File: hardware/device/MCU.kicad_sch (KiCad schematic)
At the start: 20 parts, among them J4 EXPANSION, SW24 NRST, U18 STM32H743ZIT6

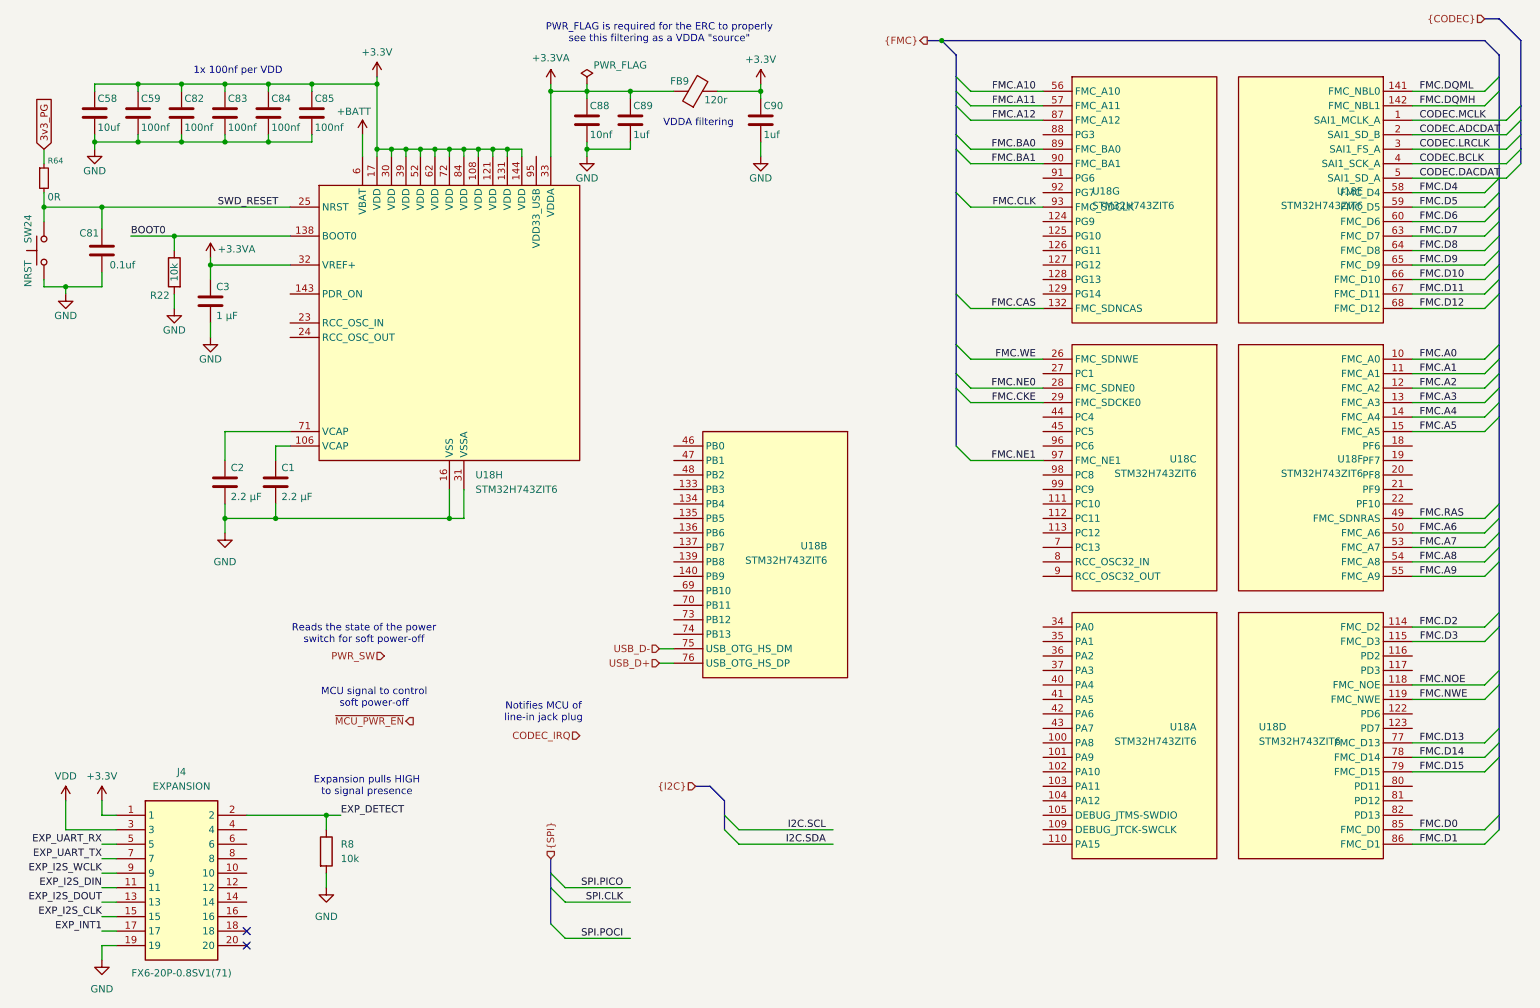
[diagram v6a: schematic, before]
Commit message: feat: change codec to NAU88C22YG
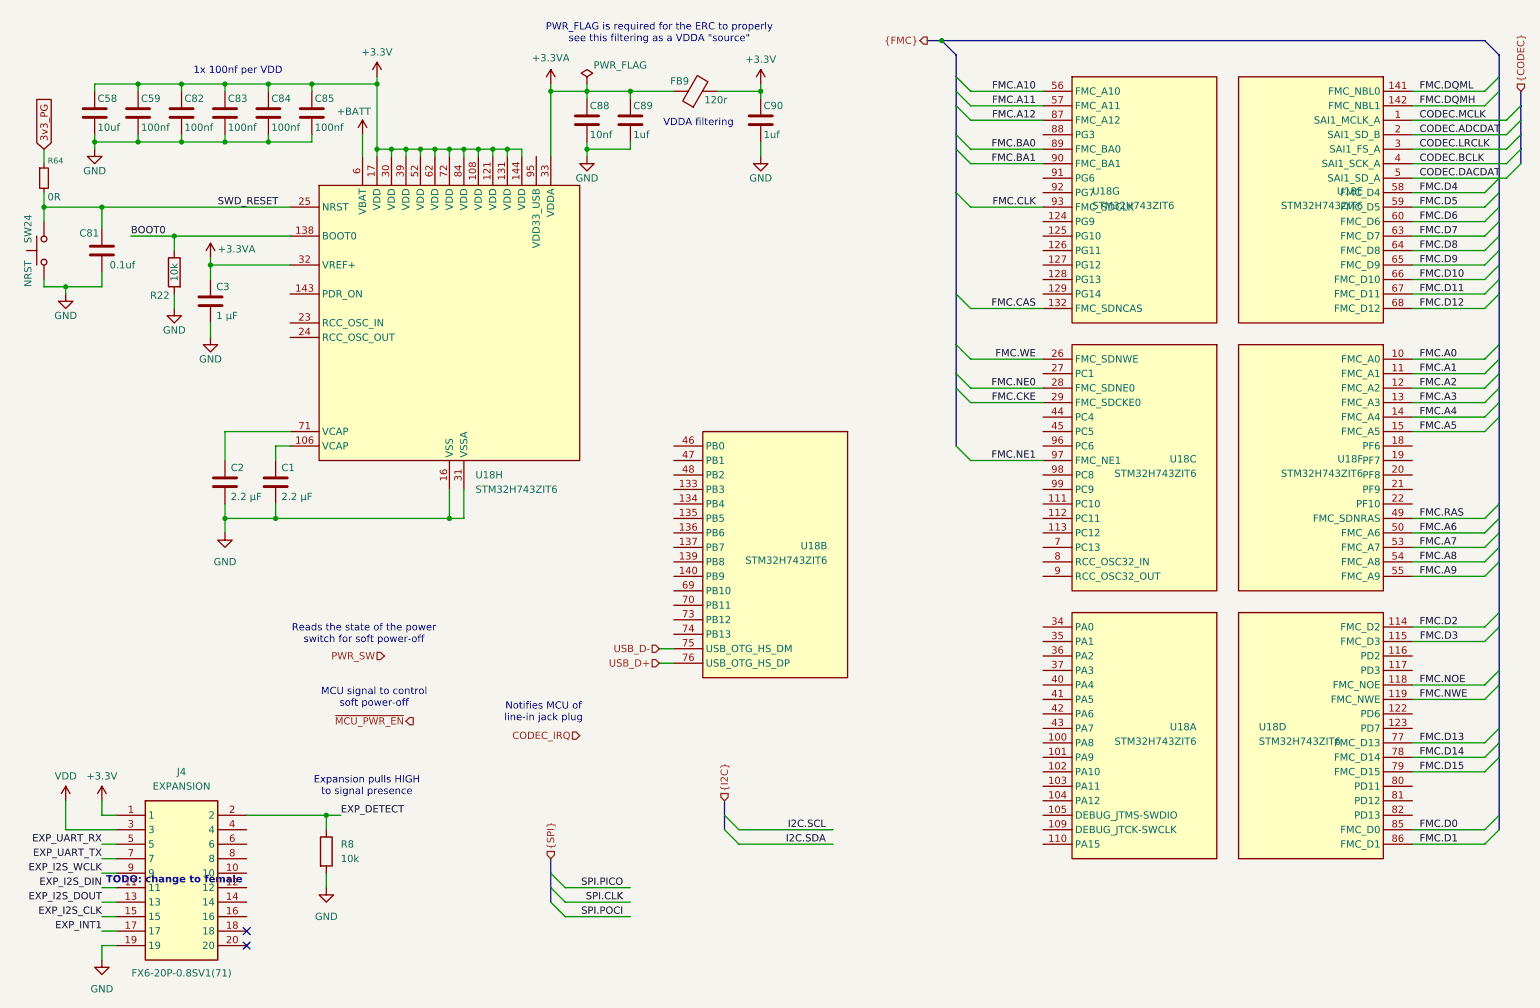
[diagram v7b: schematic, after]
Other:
- note added: "TODO: change to female"
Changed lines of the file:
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@@
 		)
 	)
+	(text "TODO: change to female"
+		(exclude_from_sim no)
+		(at 43.18 166.37 0)
+		(effects
+			(font
+				(size 1.27 1.27)
+				(thickness 0.254)
+				(bold yes)
+				(color 194 0 0 1)
+			)
+		)
+	)
 	(text "Notifies MCU of\nline-in jack plug"
 		(exclude_from_sim no)
@@
 	)
 	(bus_entry
-		(at 111.76 176.53)
+		(at 111.76 172.72)
 		(size -2.54 -2.54)
 		(stroke
@@
 	(bus
 		(pts
-			(xy 134.62 149.86) (xy 137.16 149.86)
-		)
-		(stroke
-			(width 0)
-			(type default)
-		)
-	)
-	(bus
-		(pts
 			(xy 180.34 72.39) (xy 180.34 77.47)
 		)
@@
 	(wire
 		(pts
-			(xy 111.76 176.53) (xy 123.19 176.53)
+			(xy 111.76 172.72) (xy 123.19 172.72)
 		)
 		(stroke
@@
 	(bus
 		(pts
-			(xy 279.4 30.48) (xy 279.4 19.05)
+			(xy 279.4 30.48) (xy 279.4 27.94)
 		)
 		(stroke
@@
 	(bus
 		(pts
-			(xy 109.22 162.56) (xy 109.22 165.1)
-		)
-		(stroke
-			(width 0)
-			(type default)
-		)
-	)
-	(bus
-		(pts
 			(xy 273.05 19.05) (xy 275.59 21.59)
 		)
@@
 		)
 	)
+	(bus
+		(pts
+			(xy 109.22 165.1) (xy 109.22 167.64)
+		)
+		(stroke
+			(width 0)
+			(type default)
+		)
+	)
 	(wire
 		(pts
@@
 		)
 	)
-	(bus
-		(pts
-			(xy 139.7 152.4) (xy 137.16 149.86)
-		)
-		(stroke
-			(width 0)
-			(type default)
-		)
-	)
 	(wire
 		(pts
@@
 		)
 	)
-	(bus
-		(pts
-			(xy 109.22 165.1) (xy 109.22 167.64)
-		)
-		(stroke
-			(width 0)
-			(type default)
-		)
-	)
 	(wire
 		(pts
@@
 		)
 	)
-	(bus
-		(pts
-			(xy 279.4 19.05) (xy 275.59 15.24)
-		)
-		(stroke
-			(width 0)
-			(type default)
-		)
-	)
 	(wire
 		(pts
@@
 		)
 	)
+	(bus
+		(pts
+			(xy 109.22 167.64) (xy 109.22 170.18)
+		)
+		(stroke
+			(width 0)
+			(type default)
+		)
+	)
 	(wire
 		(pts
@@
 	(bus
 		(pts
-			(xy 109.22 167.64) (xy 109.22 173.99)
+			(xy 109.22 162.56) (xy 109.22 165.1)
 		)
 		(stroke
@@
 		)
 	)
-	(bus
-		(pts
-			(xy 273.05 15.24) (xy 275.59 15.24)
-		)
-		(stroke
-			(width 0)
-			(type default)
-		)
-	)
 	(wire
 		(pts
@@
 	)
 	(label "SPI.POCI"
-		(at 121.92 176.53 180)
+		(at 121.92 172.72 180)
 		(effects
 			(font
@@
 	(hierarchical_label "{I2C}"
 		(shape input)
-		(at 134.62 149.86 180)
+		(at 139.7 152.4 90)
 		(effects
 			(font
 				(size 1.27 1.27)
 			)
-			(justify right)
+			(justify left)
 		)
 	)
@@
 	(hierarchical_label "{CODEC}"
 		(shape input)
-		(at 273.05 15.24 180)
+		(at 279.4 27.94 90)
 		(effects
 			(font
 				(size 1.27 1.27)
 			)
-			(justify right)
+			(justify left)
 		)
 	)

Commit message: feat: various PCB layout and routing
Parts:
- C1, C2, C3, C58, C59, C81, C82, C83, C84, C85, C88, C89, C90: footprint Capacitor_SMD:C_0603_1608Metric_Pad1.08x0.95mm_HandSolder -> Capacitor_SMD:C_0402_1005Metric
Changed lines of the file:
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@@
 			)
 		)
-		(property "Footprint" "Capacitor_SMD:C_0603_1608Metric_Pad1.08x0.95mm_HandSolder"
+		(property "Footprint" "Capacitor_SMD:C_0402_1005Metric"
 			(at 61.9252 100.33 0)
 			(effects
@@
 			)
 		)
-		(property "Footprint" "Capacitor_SMD:C_0603_1608Metric_Pad1.08x0.95mm_HandSolder"
+		(property "Footprint" "Capacitor_SMD:C_0402_1005Metric"
 			(at 124.1552 36.83 0)
 			(effects
@@
 			)
 		)
-		(property "Footprint" "Capacitor_SMD:C_0603_1608Metric_Pad1.08x0.95mm_HandSolder"
+		(property "Footprint" "Capacitor_SMD:C_0402_1005Metric"
 			(at 45.4152 35.56 0)
 			(effects
@@
 			)
 		)
-		(property "Footprint" "Capacitor_SMD:C_0603_1608Metric_Pad1.08x0.95mm_HandSolder"
+		(property "Footprint" "Capacitor_SMD:C_0402_1005Metric"
 			(at 147.0152 36.83 0)
 			(effects
@@
 			)
 		)
-		(property "Footprint" "Capacitor_SMD:C_0603_1608Metric_Pad1.08x0.95mm_HandSolder"
+		(property "Footprint" "Capacitor_SMD:C_0402_1005Metric"
 			(at 50.4952 68.58 0)
 			(effects
@@
 			)
 		)
-		(property "Footprint" "Capacitor_SMD:C_0603_1608Metric_Pad1.08x0.95mm_HandSolder"
+		(property "Footprint" "Capacitor_SMD:C_0402_1005Metric"
 			(at 53.0352 100.33 0)
 			(effects
@@
 			)
 		)
-		(property "Footprint" "Capacitor_SMD:C_0603_1608Metric_Pad1.08x0.95mm_HandSolder"
+		(property "Footprint" "Capacitor_SMD:C_0402_1005Metric"
 			(at 116.5352 36.83 0)
 			(effects
@@
 			)
 		)
-		(property "Footprint" "Capacitor_SMD:C_0603_1608Metric_Pad1.08x0.95mm_HandSolder"
+		(property "Footprint" "Capacitor_SMD:C_0402_1005Metric"
 			(at 68.2752 35.56 0)
 			(effects
@@
 			)
 		)
-		(property "Footprint" "Capacitor_SMD:C_0603_1608Metric_Pad1.08x0.95mm_HandSolder"
+		(property "Footprint" "Capacitor_SMD:C_0402_1005Metric"
 			(at 29.5148 52.07 0)
 			(effects
@@
 			)
 		)
-		(property "Footprint" "Capacitor_SMD:C_0603_1608Metric_Pad1.08x0.95mm_HandSolder"
+		(property "Footprint" "Capacitor_SMD:C_0402_1005Metric"
 			(at 53.0352 35.56 0)
 			(effects
@@
 			)
 		)
-		(property "Footprint" "Capacitor_SMD:C_0603_1608Metric_Pad1.08x0.95mm_HandSolder"
+		(property "Footprint" "Capacitor_SMD:C_0402_1005Metric"
 			(at 37.7952 35.56 0)
 			(effects
@@
 			)
 		)
-		(property "Footprint" "Capacitor_SMD:C_0603_1608Metric_Pad1.08x0.95mm_HandSolder"
+		(property "Footprint" "Capacitor_SMD:C_0402_1005Metric"
 			(at 30.1752 35.56 0)
 			(effects
@@
 			)
 		)
-		(property "Footprint" "Capacitor_SMD:C_0603_1608Metric_Pad1.08x0.95mm_HandSolder"
+		(property "Footprint" "Capacitor_SMD:C_0402_1005Metric"
 			(at 60.6552 35.56 0)
 			(effects
